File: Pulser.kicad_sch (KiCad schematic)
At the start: 1 part, among them J5 5499922-4

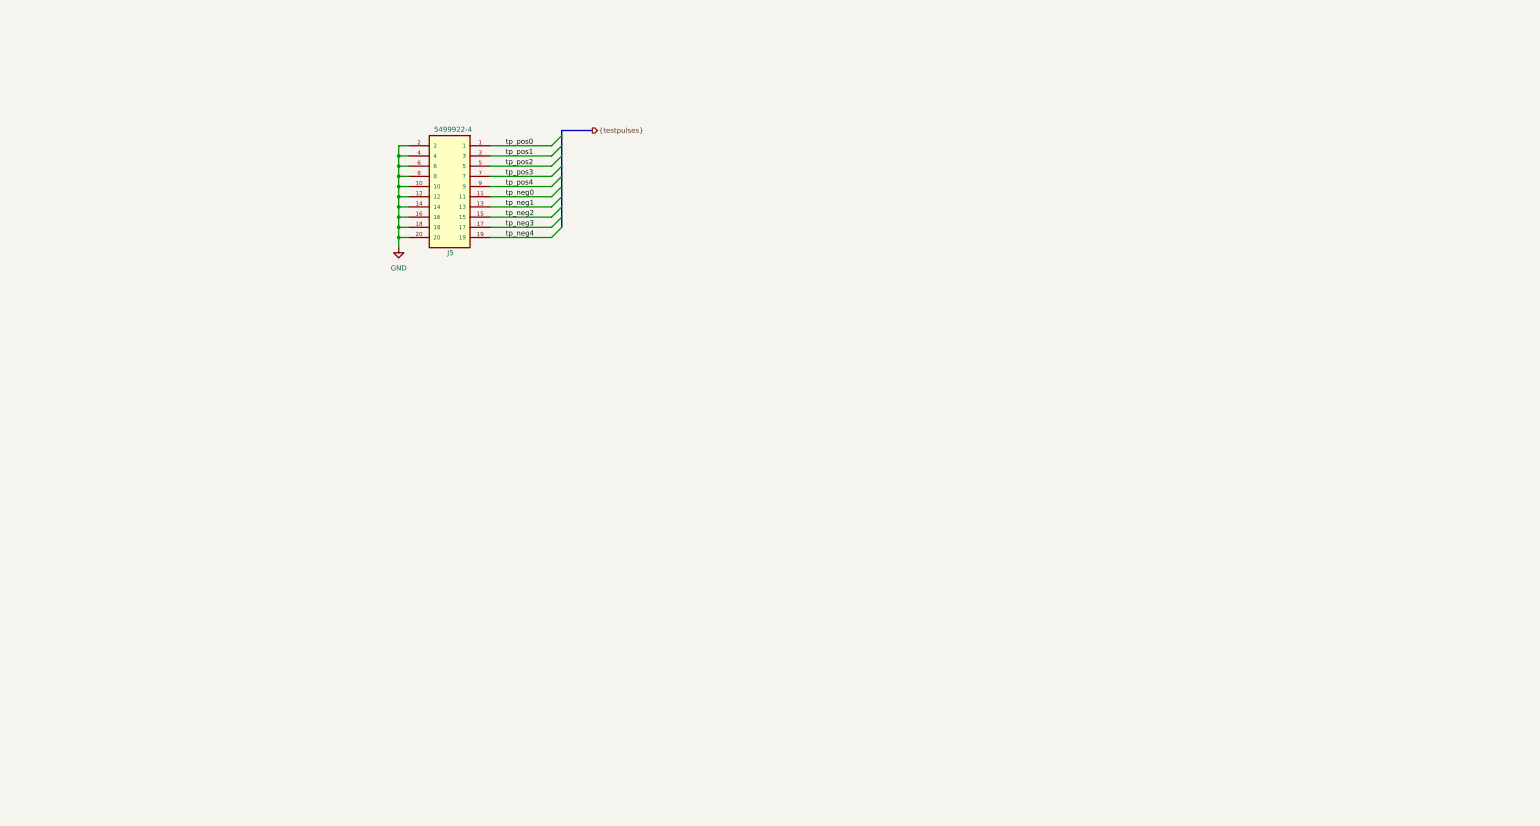
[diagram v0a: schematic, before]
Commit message: adding pulser to afe board
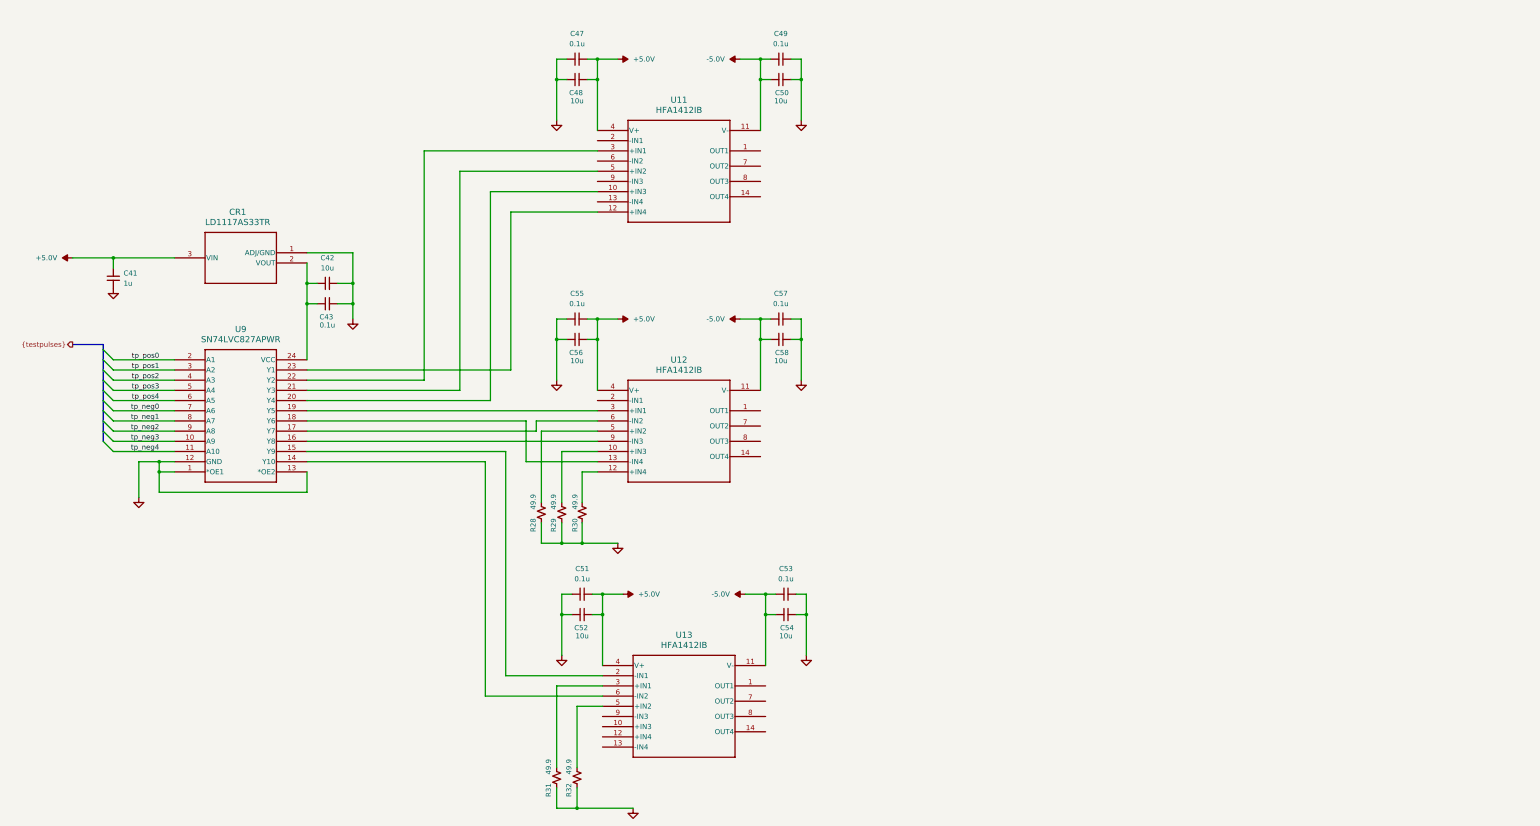
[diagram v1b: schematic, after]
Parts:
- removed J5: 5499922-4, My Footprints:TE_5499922-4, symbol My Symbols:5499922-4
- added C41: 1u, Capacitor_SMD:C_0805_2012Metric, symbol Device:C_Small
- added C42, C48, C50, C52, C54, C56, C58: 10u, Capacitor_SMD:C_0805_2012Metric, symbol Device:C_Small
- added C43, C47, C49, C51, C53, C55, C57: 0.1u, Capacitor_SMD:C_0805_2012Metric, symbol Device:C_Small
- added CR1: LD1117AS33TR, SOT-223_STM, symbol 2026-10-06_14-20-56:LD1117AS33TR
- added R28, R29, R30, R31, R32: 49.9, Resistor_SMD:R_0805_2012Metric, symbol Device:R_Small_US
- added U11, U12, U13: HFA1412IB, SOIC14_4X8P75_INR, symbol 2026-10-06_14-17-31:HFA1412IB
- added U9: SN74LVC827APWR, PW24, symbol 2026-10-06_14-22-36:SN74LVC827APWR
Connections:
- net GND: now also C41.2, C42.2, C43.2, C47.1, C48.1, C49.1, C50.1, C51.1, C52.1, C53.1, C54.1, C55.1, C56.1, C57.1, C58.1, CR1.1 (ADJ/GND), R28.2, R29.2, R30.2, R31.2, R32.2, U9.1 (*OE1), U9.12 (GND), U9.13 (*OE2)
- net tp_neg0: now also U9.7 (A6)
- net tp_neg1: now also U9.8 (A7)
- net tp_neg2: now also U9.9 (A8)
- net tp_neg3: now also U9.10 (A9)
- net tp_neg4: now also U9.11 (A10)
- net tp_pos0: now also U9.2 (A1)
- net tp_pos1: now also U9.3 (A2)
- net tp_pos2: now also U9.4 (A3)
- net tp_pos3: now also U9.5 (A4)
- net tp_pos4: now also U9.6 (A5)
- new net: R32.1, U13.5 (+IN2)
- new net: R29.1, U12.10 (+IN3)
- new net: R30.1, U12.12 (+IN4)
- new net: U12.13 (-IN4), U9.18 (Y6)
- new net: U12.3 (+IN1), U9.19 (Y5)
- new net: R28.1, U12.5 (+IN2)
- new net: U12.6 (-IN2), U9.17 (Y7)
- new net: U12.9 (-IN3), U9.16 (Y8)
- new net: U11.10 (+IN3), U9.20 (Y4)
- new net: U11.12 (+IN4), U9.23 (Y1)
- new net: U11.3 (+IN1), U9.22 (Y2)
- new net: U11.5 (+IN2), U9.21 (Y3)
- new net: U13.6 (-IN2), U9.14 (Y10)
- new net: U13.2 (-IN1), U9.15 (Y9)
- new net: C42.1, C43.1, CR1.2 (VOUT), U9.24 (VCC)
- new net: R31.1, U13.3 (+IN1)
- new net +5.0V: C41.1, C47.2, C48.2, C51.2, C52.2, C55.2, C56.2, CR1.3 (VIN), U11.4 (V+), U12.4 (V+), U13.4 (V+)
- new net -5.0V: C49.2, C50.2, C53.2, C54.2, C57.2, C58.2, U11.11 (V-), U12.11 (V-), U13.11 (V-)

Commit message: added pulser to afe and spi interface for arduino
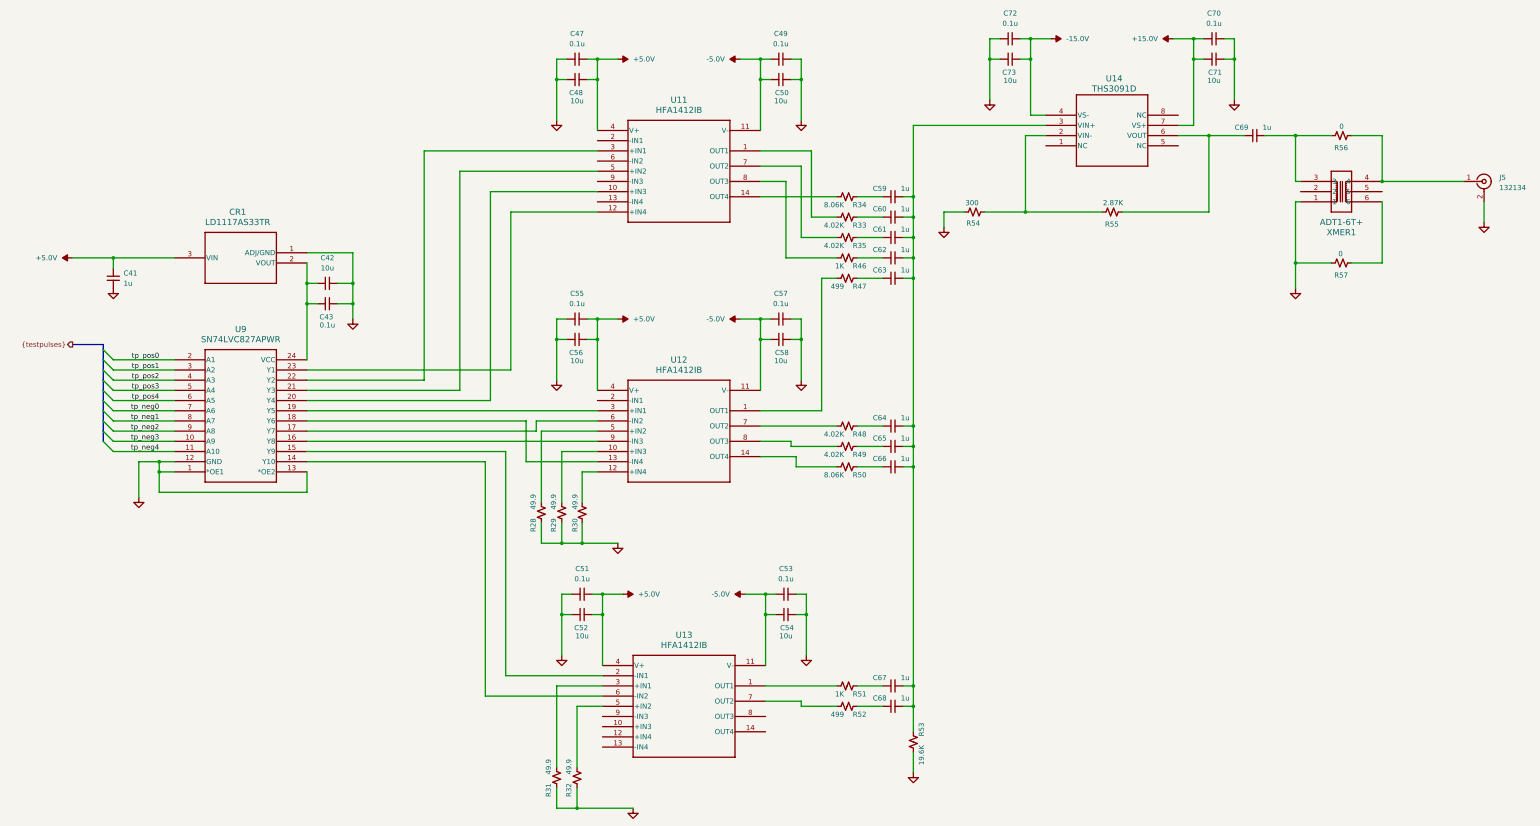
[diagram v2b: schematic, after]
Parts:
- added C59, C60, C61, C62, C63, C64, C65, C66, C67, C68, C69: 1u, Capacitor_SMD:C_0805_2012Metric, symbol Device:C_Small
- added C70, C72: 0.1u, Capacitor_SMD:C_0805_2012Metric, symbol Device:C_Small
- added C71, C73: 10u, Capacitor_SMD:C_1206_3216Metric, symbol Device:C_Small
- added J5: 132134, Connector_Coaxial:SMA_Amphenol_132134_Vertical, symbol Connector:Conn_Coaxial
- added R33, R35, R48, R49: 4.02K, Resistor_SMD:R_0805_2012Metric, symbol Device:R_Small_US
- added R34, R50: 8.06K, Resistor_SMD:R_0805_2012Metric, symbol Device:R_Small_US
- added R46, R51: 1K, Resistor_SMD:R_0805_2012Metric, symbol Device:R_Small_US
- added R47, R52: 499, Resistor_SMD:R_0805_2012Metric, symbol Device:R_Small_US
- added R53: 19.6K, Resistor_SMD:R_0805_2012Metric, symbol Device:R_Small_US
- added R54: 300, Resistor_SMD:R_0805_2012Metric, symbol Device:R_Small_US
- added R55: 2.87K, Resistor_SMD:R_0805_2012Metric, symbol Device:R_Small_US
- added R56, R57: 0, Resistor_SMD:R_0805_2012Metric, symbol Device:R_Small_US
- added U14: THS3091D, ths3091d:D8, symbol 2026-10-06_14-20-19:THS3091D
- added XMER1: ADT1-6T+, adt1-6+:CD637_MNC, symbol 2026-10-05_18-52-29:ADT1-6T+
- C43, C48, C50, C52, C54, C56, C58: footprint Capacitor_SMD:C_0805_2012Metric -> Capacitor_SMD:C_1206_3216Metric
- CR1: footprint SOT-223_STM -> ld1117as33tr:SOT-223_STM
- U11, U12, U13: footprint SOIC14_4X8P75_INR -> hfa1412ib:SOIC14_4X8P75_INR
- U9: footprint PW24 -> sn74lvc827:PW24
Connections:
- net GND: now also C70.1, C71.1, C72.1, C73.1, J5.2 (Ext), R53.1, R54.2, R57.2, XMER1.1
- net at U12.1 (OUT1): now also R47.1
- net at U12.14 (OUT4): now also R50.1
- net at U12.7 (OUT2): now also R48.1
- net at U12.8 (OUT3): now also R49.1
- net at U11.1 (OUT1): now also R33.1
- net at U11.14 (OUT4): now also R34.1
- net at U11.7 (OUT2): now also R35.1
- net at U11.8 (OUT3): now also R46.1
- net at U13.1 (OUT1): now also R51.1
- net at U13.7 (OUT2): now also R52.1
- new net: C63.1, R47.2
- new net: C59.2, C60.2, C61.2, C62.2, C63.2, C64.2, C65.2, C66.2, C67.2, C68.2, R53.2, U14.3 (VIN+)
- new net: C66.1, R50.2
- new net: C68.1, R52.2
- new net: C69.1, R55.1, U14.6 (VOUT)
- new net: C69.2, R56.2, XMER1.3
- new net: C61.1, R35.2
- new net: R54.1, R55.2, U14.2 (VIN-)
- new net: C62.1, R46.2
- new net: C59.1, R34.2
- new net: C65.1, R49.2
- new net: C67.1, R51.2
- new net: C60.1, R33.2
- new net: J5.1 (In), R56.1, XMER1.4
- new net: R57.1, XMER1.6
- new net: C64.1, R48.2
- new net +15.0V: C70.2, C71.2, U14.7 (VS+)
- new net -15.0V: C72.2, C73.2, U14.4 (VS-)
